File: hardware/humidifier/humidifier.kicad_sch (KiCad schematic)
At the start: 7 parts, among them J1 Conn_01x02_Pin, Q1 Q_NMOS_GSD

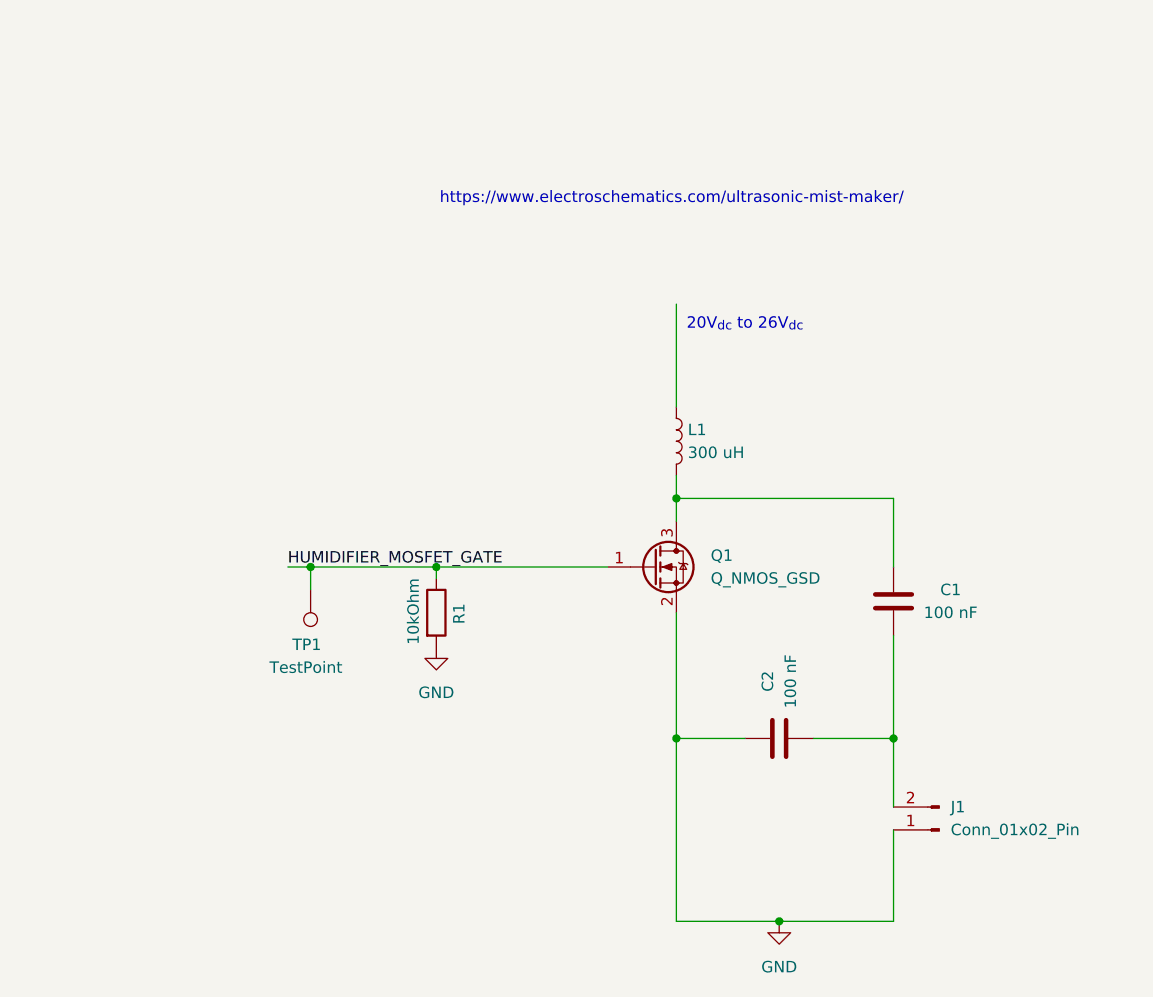
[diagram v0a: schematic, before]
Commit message: Update humidifier circuit
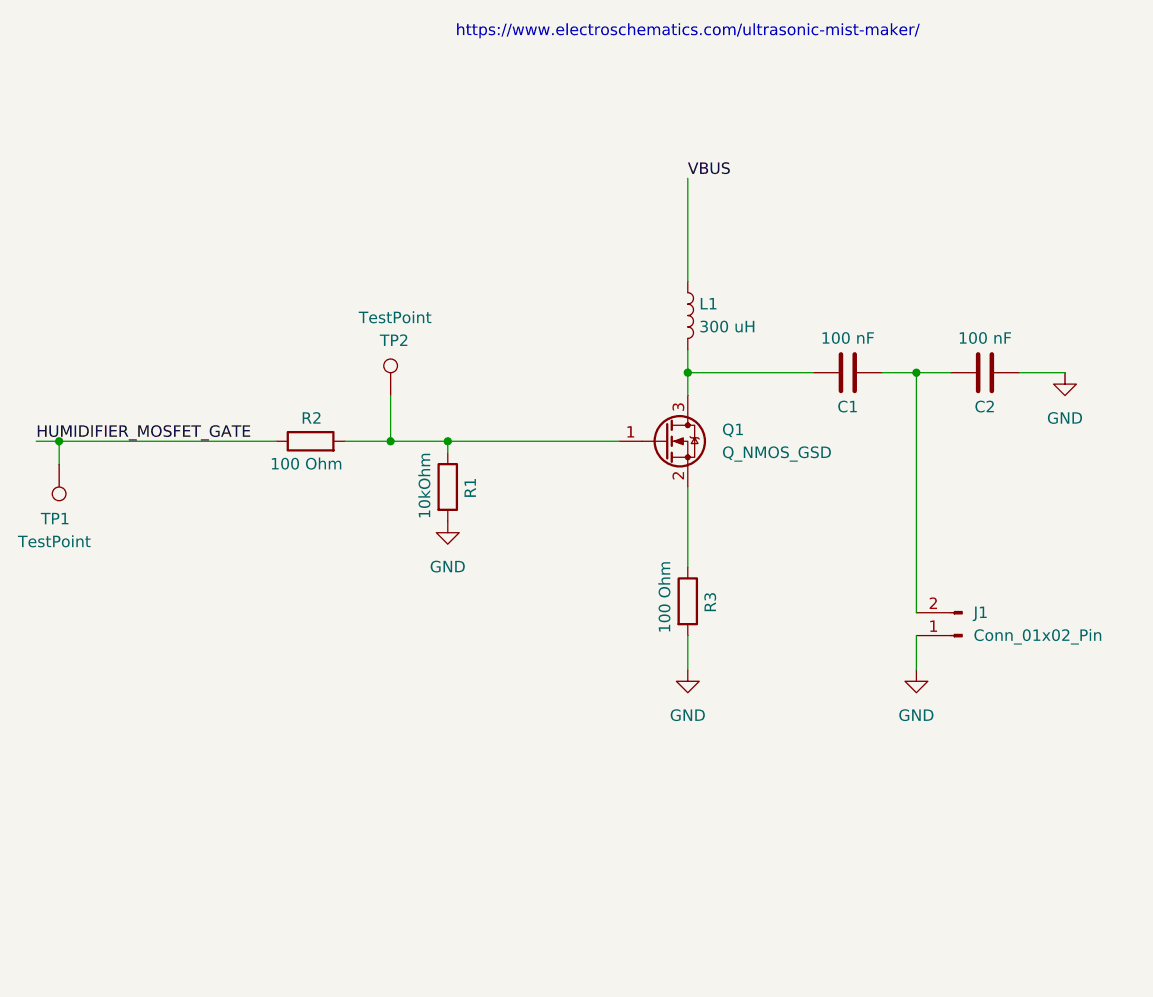
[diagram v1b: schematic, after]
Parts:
- added R2, R3: 100 Ohm, Resistor_SMD:R_0603_1608Metric, symbol Device:R
- added TP2: TestPoint, E7020E:TestPoint_THTPad_1.5x1.5mm_Drill0.8mm, symbol Connector:TestPoint
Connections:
- net GND: now also C2.2, R3.2; no longer C2.1, Q1.2 (S)
- net HUMIDIFIER_MOSFET_GATE: now also R2.1; no longer Q1.1 (G), R1.1
- net VBUS: now reaches L1.1
- net at C1.2, J1.2 (Pin_2): now also C2.1; no longer C2.2
- new net: Q1.1 (G), R1.1, R2.2, TP2.1
- new net: Q1.2 (S), R3.1
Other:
- note removed: "20V_{dc} to 26V_{dc}"
- moved on the sheet: C1, J1, L1, Q1, R1, TP1
